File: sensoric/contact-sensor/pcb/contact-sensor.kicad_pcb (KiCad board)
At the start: 2 copper layers, 66 x 20.3 mm, 9 parts, among them J1 Conn_01x02_Male, J2 Conn_01x02_Male, SW1 SW_Push, SW2 SW_Push, SW3 SW_Push

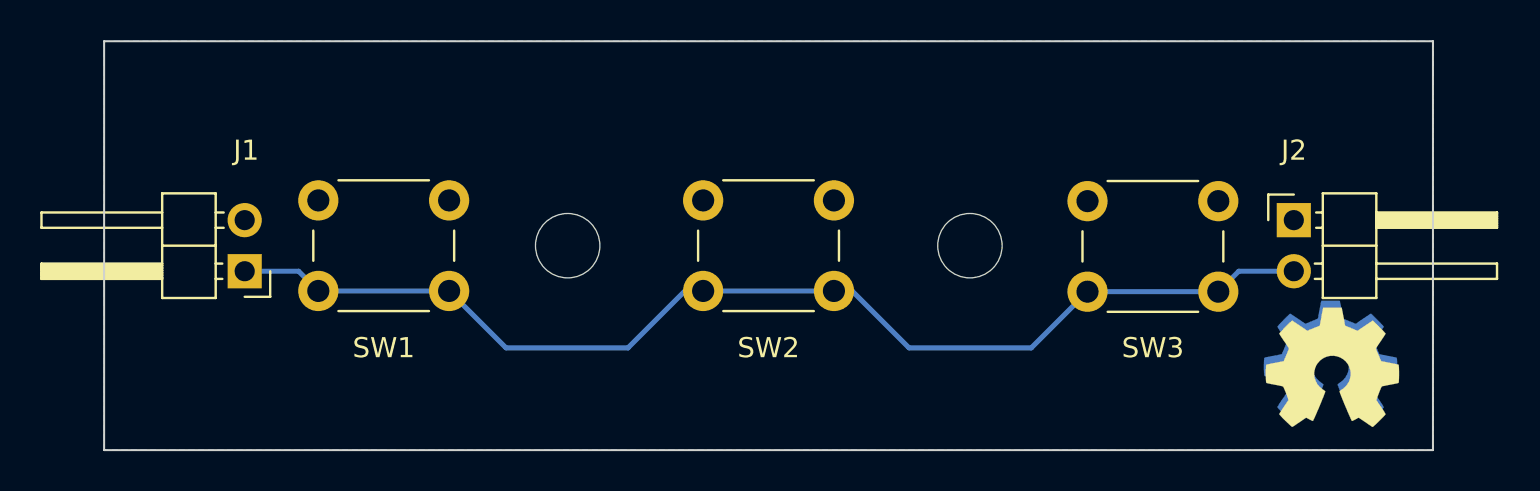
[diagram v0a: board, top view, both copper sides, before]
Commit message: refactor: changed connection pin position for better chaining
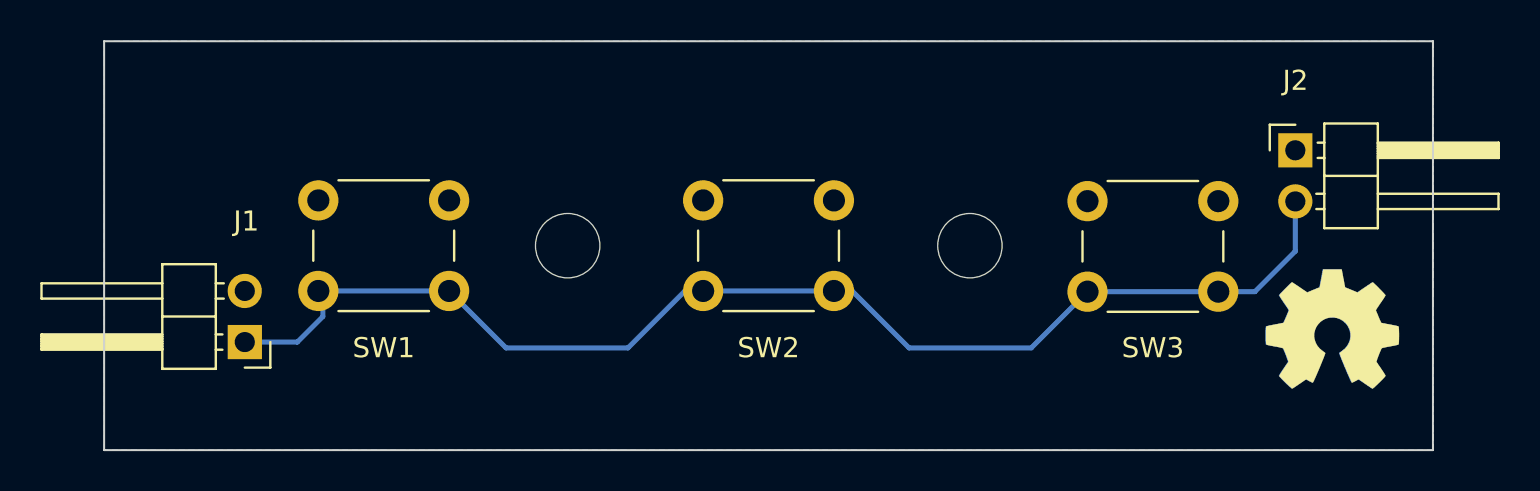
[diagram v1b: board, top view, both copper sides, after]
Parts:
- moved J1 3.52 mm to (46.9, 99.1)
- moved J2 3.47 mm to (99.1, 89.5)
- moved REF** 1.91 mm to (101.0, 98.4)
- moved REF3 1.56 mm to (101.0, 98.4)
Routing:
- net +5V: track 57.6 -> 62.3 mm
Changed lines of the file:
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@@
   (title_block
     (title "Contact sensor")
-    (date "2022-03-07")
-    (rev "0.1.0")
+    (date "2022-03-08")
+    (rev "0.1.1")
     (comment 1 "https://github.com/atlas144/mals")
     (comment 2 "SPDX-License-Identifier: CERN-OHL-S-2.0")
@@
   (net 2 "+5V")
   (footprint "Connector_PinHeader_2.54mm:PinHeader_1x02_P2.54mm_Horizontal" (layer "F.Cu")
-    (at 99.055 93)
+    (at 99.13 89.53)
     (descr "Through hole angled pin header, 1x02, 2.54mm pitch, 6mm pin length, single row")
     (tags "Through hole angled pin header THT 1x02 2.54mm single row")
@@
   )
   (footprint "Connector_PinHeader_2.54mm:PinHeader_1x02_P2.54mm_Horizontal" (layer "F.Cu")
-    (at 46.915 95.54 180)
+    (at 46.92 99.06 180)
     (descr "Through hole angled pin header, 1x02, 2.54mm pitch, 6mm pin length, single row")
     (tags "Through hole angled pin header THT 1x02 2.54mm single row")
@@
   )
   (footprint "Symbol:OSHW-Symbol_6.7x6mm_SilkScreen" (layer "F.Cu")
-    (at 100.965 100.33)
+    (at 100.965 98.425)
     (descr "Open Source Hardware Symbol")
     (tags "Logo Symbol OSHW")
@@
   )
   (footprint "Symbol:OSHW-Symbol_6.7x6mm_Copper" (layer "B.Cu")
-    (at 100.89 99.985 180)
+    (at 100.965 98.425 180)
     (descr "Open Source Hardware Symbol")
     (tags "Logo Symbol OSHW")
@@
   (segment (start 69.7 96.52) (end 76.2 96.52) (width 0.25) (layer "B.Cu") (net 2))
   (segment (start 68.795 96.52) (end 69.7 96.52) (width 0.25) (layer "B.Cu") (net 2))
-  (segment (start 96.318 95.54) (end 95.302 96.556) (width 0.25) (layer "B.Cu") (net 2))
-  (segment (start 49.595 95.54) (end 50.575 96.52) (width 0.25) (layer "B.Cu") (net 2))
+  (segment (start 49.53 99.06) (end 50.8 97.79) (width 0.25) (layer "B.Cu") (net 2))
+  (segment (start 50.8 97.79) (end 50.8 96.745) (width 0.25) (layer "B.Cu") (net 2))
+  (segment (start 97.119 96.556) (end 99.13 94.545) (width 0.25) (layer "B.Cu") (net 2))
   (segment (start 65.965 99.35) (end 68.795 96.52) (width 0.25) (layer "B.Cu") (net 2))
-  (segment (start 46.915 95.54) (end 49.595 95.54) (width 0.25) (layer "B.Cu") (net 2))
+  (segment (start 50.8 96.745) (end 50.575 96.52) (width 0.25) (layer "B.Cu") (net 2))
+  (segment (start 97.119 96.556) (end 95.302 96.556) (width 0.25) (layer "B.Cu") (net 2))
   (segment (start 86.008 99.35) (end 79.935 99.35) (width 0.25) (layer "B.Cu") (net 2))
-  (segment (start 99.055 95.54) (end 96.318 95.54) (width 0.25) (layer "B.Cu") (net 2))
   (segment (start 57.075 96.52) (end 59.905 99.35) (width 0.25) (layer "B.Cu") (net 2))
+  (segment (start 46.92 99.06) (end 49.53 99.06) (width 0.25) (layer "B.Cu") (net 2))
   (segment (start 50.575 96.52) (end 57.075 96.52) (width 0.25) (layer "B.Cu") (net 2))
   (segment (start 77.105 96.52) (end 76.2 96.52) (width 0.25) (layer "B.Cu") (net 2))
+  (segment (start 99.13 94.545) (end 99.13 92.07) (width 0.25) (layer "B.Cu") (net 2))
   (segment (start 88.802 96.556) (end 86.008 99.35) (width 0.25) (layer "B.Cu") (net 2))
   (segment (start 79.935 99.35) (end 77.105 96.52) (width 0.25) (layer "B.Cu") (net 2))
